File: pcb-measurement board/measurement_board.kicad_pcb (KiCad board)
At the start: 4 copper layers, 60 x 45 mm, 78 parts, among them P1 CONN_02X15, P2 CONN_02X13, P3 HDR DUAL ROW, P4 CONN_02X05, P5 CONN_02X05, Q2 Si1101X, U1 TPS73125, U10 AD8603, U11 TLV1G125, U12 MCP4921, U13 TPS73133, U14 MCP4921, U15 74CBTLV3253, U16 AD8293, U17 NX3L4051, U18 NX3L4051, U19 QS4A110, U2 NX3L4051, U20 QS4A110, U21 QS4A110, U3 NX3L4051, U4 NX3L4051, U5 MSP430G2955, U6 TLV1G125, U7 NX3L4051, U8 AD8603, U9 TLV1G125

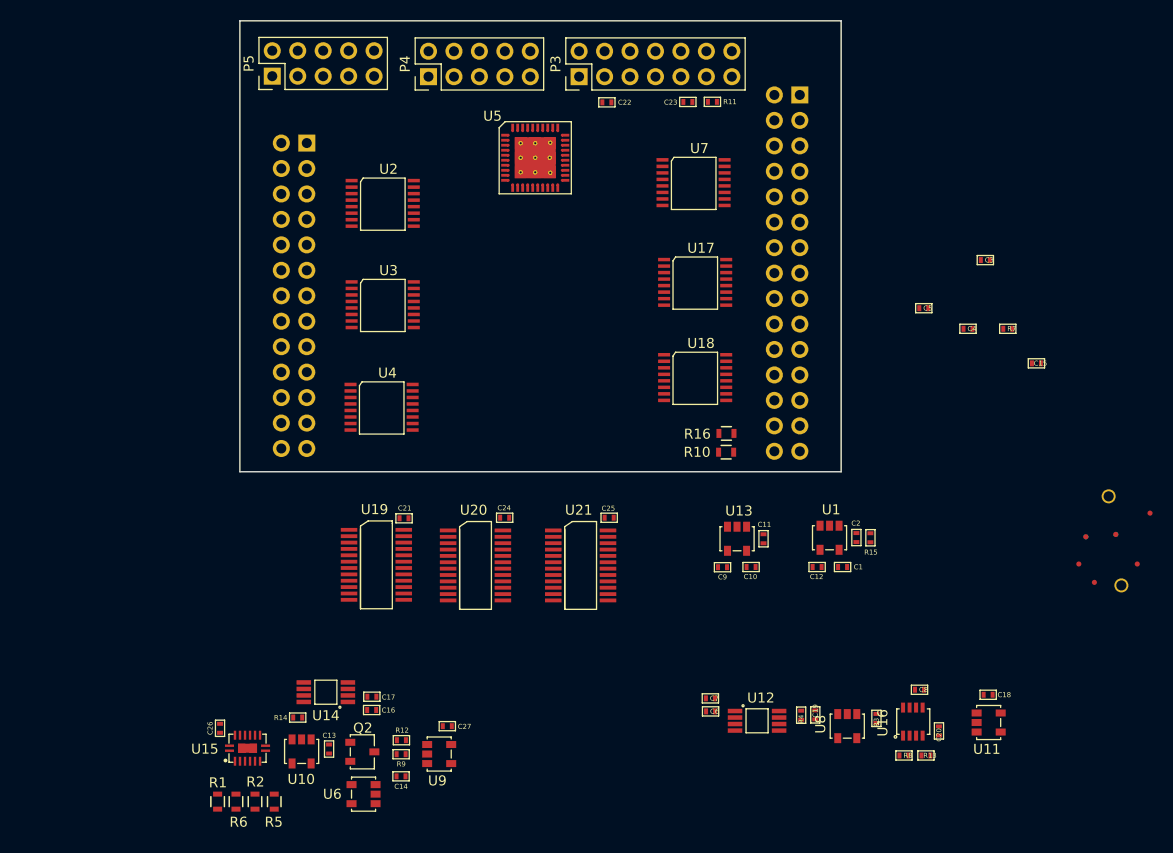
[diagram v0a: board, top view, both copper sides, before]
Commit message: -component placement completed -routing just started
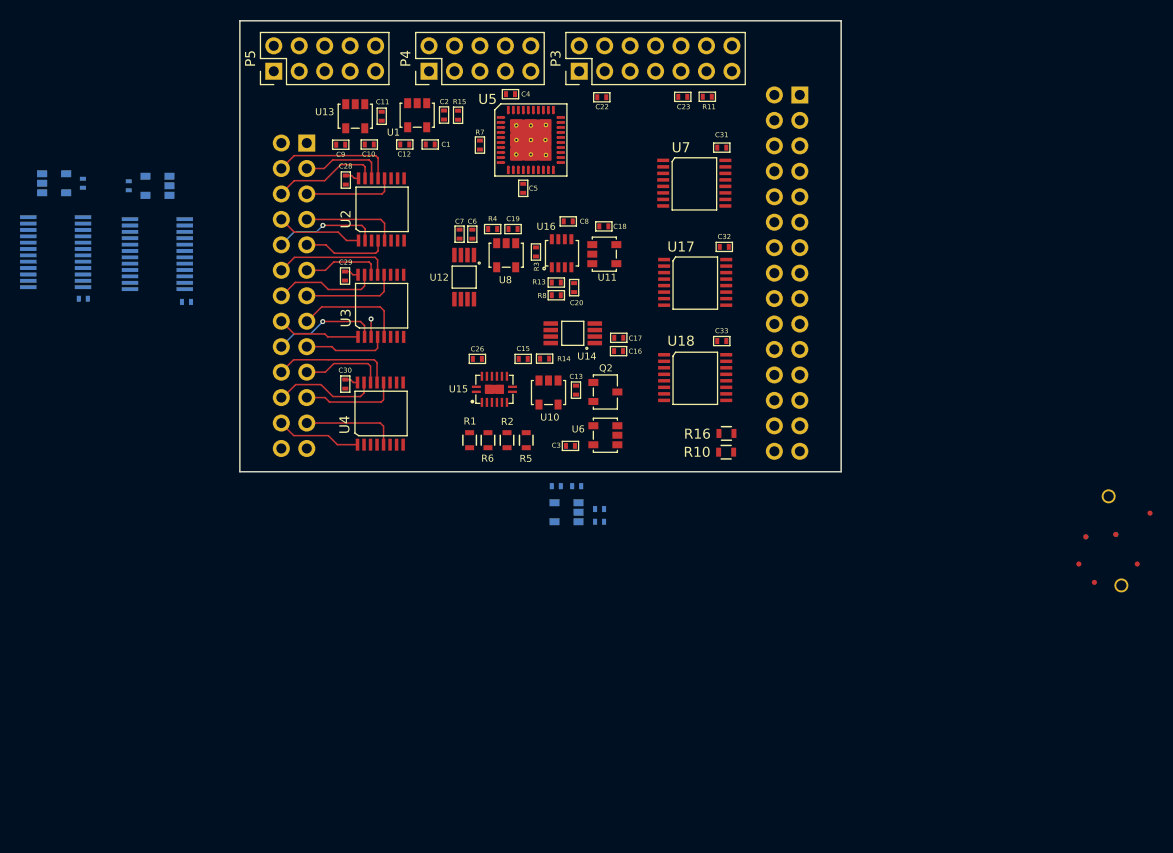
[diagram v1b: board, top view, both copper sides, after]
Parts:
- added C28: 0.1uF, footprints_on_Cdrive:0402, F.Cu at (-19.4, -9.11)
- added C29: 0.1uF, footprints_on_Cdrive:0402, F.Cu at (-19.5, 0.47)
- added C30: 0.1uF, footprints_on_Cdrive:0402, F.Cu at (-19.5, 11.3)
- added C31: 0.1uF, footprints_on_Cdrive:0402, F.Cu at (18.1, -12.3)
- added C32: 0.1uF, footprints_on_Cdrive:0402, F.Cu at (18.3, -2.44)
- added C33: 0.1uF, footprints_on_Cdrive:0402, F.Cu at (18.1, 6.96)
- added C34: 0.1uF, footprints_on_Cdrive:0402, B.Cu at (-41.1, -8.53)
- added U22: TLV1G125, footprints_on_Cdrive:SOT23-5, B.Cu at (-37.0, -8.53)
- C14, C21, C24, C25, C27, R12, R9, U19, U20, U9: moved to B.Cu
- U21: value QS4A110 -> TLV1G125; footprint footprints_on_Cdrive:QSOP-24 -> footprints_on_Cdrive:SOT23-5; moved to B.Cu
- moved C25 62.2 mm to (-45.7, -8.79), turned to 270 degrees
- moved U21 61.7 mm to (-49.7, -8.79)
- moved C18 60.5 mm to (6.31, -4.48)
- moved U11 60.5 mm to (5.16, -1.71)
- moved R13 59.9 mm to (1.57, 1.12), turned to 180 degrees
- moved C2 58.9 mm to (-9.63, -15.6)
- moved U1 58.9 mm to (-12.3, -16.8)
- moved C1 58.9 mm to (-11.0, -12.7)
- moved C12 58.9 mm to (-13.5, -12.7)
- moved R15 58.9 mm to (-8.23, -15.6)
- moved C8 58.4 mm to (2.77, -4.98)
- moved U16 58.4 mm to (1.13, -1.80)
- moved U8 58.0 mm to (-3.43, -2.81)
- moved R3 57.6 mm to (-0.46, -1.93)
- moved R8 57.6 mm to (1.57, 2.39)
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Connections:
- net Net-(U11-Pad4) renamed /Vmeas
- C25 pad 1: /5V -> /3V3
- U20 pad 11: /O2 -> /P2
- U20 pad 14: /P2 -> /Q2
- U20 pad 17: /Q2 -> /R2
- U20 pad 18: /R2 -> /S2
- U20 pad 21: /S2 -> /T2
- U20 pad 22: /T2 -> /U2
- U20 pad 3: /K2 -> /L2
- U20 pad 4: /L2 -> /M2
- U20 pad 7: /M2 -> /N2
- U20 pad 8: /N2 -> /O2
- U21 pad 2: GND -> /K2
- U21 pad 3: /U2 -> GND
- U21 pad 4: /V2 -> GND
- U21 pad 5: GND -> /3V3
- U5 pad 12: /MUX2 -> Net-(U5-Pad12)
- U5 pad 16: /~CC_EN -> /~MUX_EN1
- U5 pad 17: Net-(U5-Pad17) -> /~CC_EN
- U5 pad 2: /~MUX_EN5 -> /~MUX_EN2
- U5 pad 22: Net-(U5-Pad22) -> /DAC1_CS
- U5 pad 25: /~MUX_EN3 -> /Imeas
- U5 pad 26: /~MUX_EN2 -> /ADC_IN
- U5 pad 27: /~MUX_EN1 -> /~MUX_EN3
- U5 pad 40: /DAC1_CS -> /~MUX_EN5
- U5 pad 6: /Imeas -> /MUX0
- U5 pad 7: /MUX0 -> /MUX1
- U5 pad 8: /MUX1 -> /MUX2
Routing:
- net /A1: track 0.00 -> 12.3 mm
- net /I1: track 0.00 -> 12.2 mm
- net /E1: track 0.00 -> 11.7 mm
- net /G2: track 0.00 -> 11.1 mm
- net /B1: track 0.00 -> 10.8 mm
- net /H1: track 0.00 -> 10.6 mm, vias 0 -> 1
- net /D1: track 0.00 -> 10.5 mm, vias 0 -> 1
- net /J1: track 0.00 -> 10.5 mm
- net /F1: track 0.00 -> 10.4 mm
- net /J2: track 0.00 -> 9.66 mm
- net /C2: track 0.00 -> 9.64 mm
- net /K2: track 0.00 -> 9.63 mm
- net /F2: track 0.00 -> 9.57 mm
- net /B2: track 0.00 -> 9.17 mm
- net /D2: track 0.00 -> 8.59 mm
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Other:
- net class Default: via_dia 0.6858 -> 0.508; via_drill 0.3302 -> 0.254
- rule via_min_drill: 0.3302 -> 0.254
- rule via_min_size: 0.6858 -> 0.508

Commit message: -replaced all measurement board 0402 components with 0603 -adjusted placement and started routing on the layout
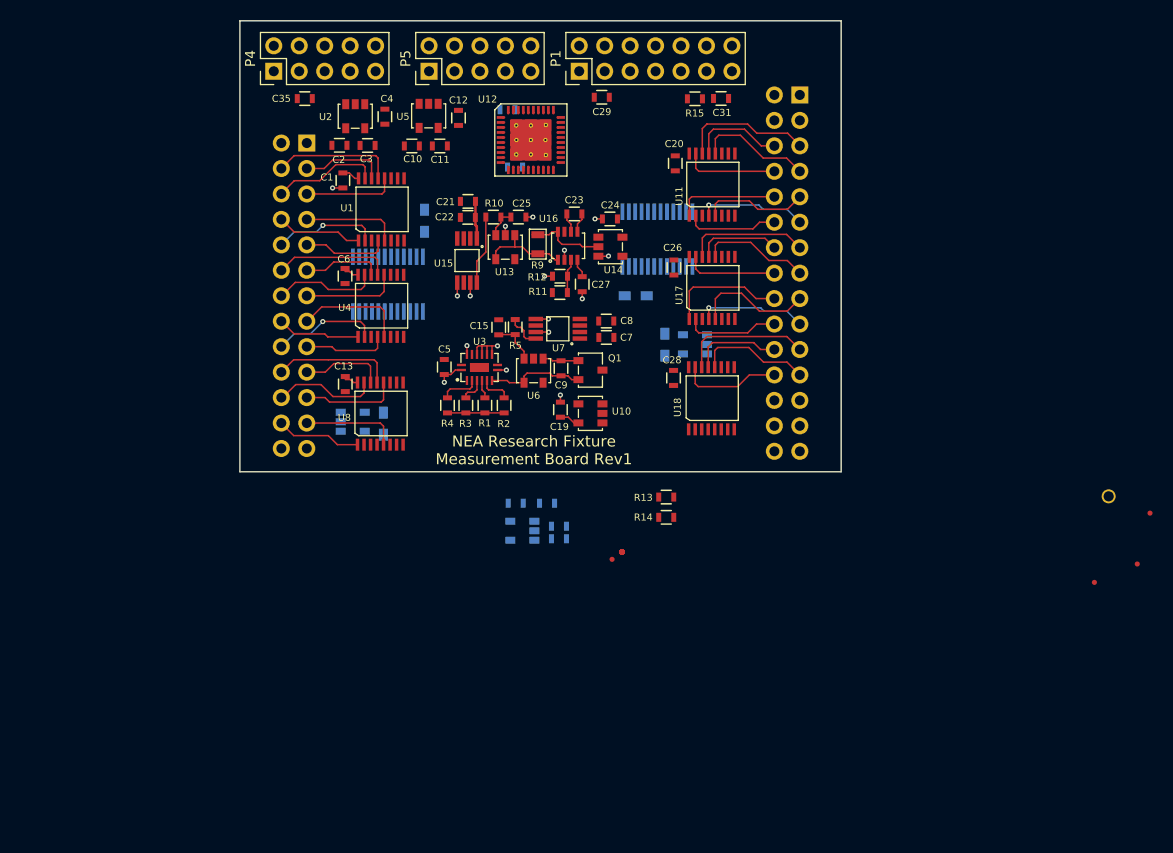
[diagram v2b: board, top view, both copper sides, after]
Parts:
- removed the R13 at (1.57, 1.12)
- removed the R14 at (0.41, 8.72)
- removed the R3 at (-0.46, -1.93)
- removed the R4 at (-4.78, -4.22)
- removed R8: 100k, footprints_on_Cdrive:0402
- removed the TP2 at (54.4, 26.5)
- removed the TP3 at (57.4, 26.3)
- removed the TP6 at (58.0, 31.3)
- added C35: 10uF, footprints_on_Cdrive:0603, F.Cu at (-23.5, -17.2)
- added R10: 1K, footprints_on_Cdrive:0603, F.Cu at (-4.71, -5.41)
- added R5: 1K, footprints_on_Cdrive:0603, F.Cu at (-2.52, 5.56)
- added R6: 1K, footprints_on_Cdrive:0603, B.Cu at (1.84, 25.4)
- added TP10, TP11, TP12, TP13, TP14, TP15, TP4, TP7, TP8, TP9: TP_SMT, footprints_on_Cdrive:TP_SMT.02, F.Cu at (8.13, 28.0)
- C1: value 0.47uF -> 0.1uF; footprint footprints_on_Cdrive:0402 -> footprints_on_Cdrive:0603
- C10, C2: value 0.47uF -> DNI; footprint footprints_on_Cdrive:0402 -> footprints_on_Cdrive:0603
- C11, C15, C19, C26, C28, C5, C8: footprint footprints_on_Cdrive:0402 -> footprints_on_Cdrive:0603
- C12: value DNI -> 0.47uF; footprint footprints_on_Cdrive:0402 -> footprints_on_Cdrive:0603
- C13: value 51pF -> 0.1uF; footprint footprints_on_Cdrive:0402 -> footprints_on_Cdrive:0603
- C14: value 1nF -> 1.1nF; footprint footprints_on_Cdrive:0402 -> footprints_on_Cdrive:0603
- C16: value 10uF -> 0.1uF; footprint footprints_on_Cdrive:0402 -> footprints_on_Cdrive:0603; moved to B.Cu
- C17, C18: footprint footprints_on_Cdrive:0402 -> footprints_on_Cdrive:0603; moved to B.Cu
- C20: value 39nF -> 0.1uF; footprint footprints_on_Cdrive:0402 -> footprints_on_Cdrive:0603
- C21: value 0.1uF -> 10uF; footprint footprints_on_Cdrive:0402 -> footprints_on_Cdrive:0603; moved to F.Cu
- C22, C6: value 10uF -> 0.1uF; footprint footprints_on_Cdrive:0402 -> footprints_on_Cdrive:0603
- C23: value 1.1nF -> 0.1uF; footprint footprints_on_Cdrive:0402 -> footprints_on_Cdrive:0603
- C24, C25: footprint footprints_on_Cdrive:0402 -> footprints_on_Cdrive:0603; moved to F.Cu
- C27: value 0.1uF -> 39nF; footprint footprints_on_Cdrive:0402 -> footprints_on_Cdrive:0603; moved to F.Cu
- C29, C7: value 0.1uF -> 10uF; footprint footprints_on_Cdrive:0402 -> footprints_on_Cdrive:0603
- C3, C4: value 0.1uF -> 0.47uF; footprint footprints_on_Cdrive:0402 -> footprints_on_Cdrive:0603
- C30, C32, C33: footprint footprints_on_Cdrive:0402 -> Resistors_SMD:R_0603_HandSoldering; moved to B.Cu
- C31: value 0.1uF -> 1.1nF; footprint footprints_on_Cdrive:0402 -> footprints_on_Cdrive:0603
- C34: footprint footprints_on_Cdrive:0402 -> Resistors_SMD:R_0603_HandSoldering
- C9: value DNI -> 51pF; footprint footprints_on_Cdrive:0402 -> footprints_on_Cdrive:0603
- R11: value 47K -> 100k; footprint footprints_on_Cdrive:0402 -> footprints_on_Cdrive:0603
- R12: value 100K -> 18k; footprint footprints_on_Cdrive:0402 -> footprints_on_Cdrive:0603; moved to F.Cu
- R15: value 1K -> 47K; footprint footprints_on_Cdrive:0402 -> footprints_on_Cdrive:0603
- R7: value 47K -> 100k; footprint footprints_on_Cdrive:0402 -> footprints_on_Cdrive:0603; moved to B.Cu
- R9: value 1K -> 10ohm 0.1%; footprint footprints_on_Cdrive:0402 -> footprints_on_Cdrive:0805; moved to F.Cu
- moved U22 55.9 mm to (16.6, 7.29)
- moved C34 55.8 mm to (12.4, 7.33), turned to 270 degrees
- moved U20 49.7 mm to (8.17, -5.95), turned to 0 degrees
- moved TP1 46.6 mm to (7.14, 28.7)
- moved C25 43.6 mm to (-2.21, -5.41), turned to 0 degrees
- moved C24 43.1 mm to (6.92, -5.23)
- moved C21 39.6 mm to (-7.24, -6.98)
- moved U19 39.4 mm to (-11.7, 4.01), turned to 180 degrees
- moved C28 38.2 mm to (13.3, 10.6), turned to 270 degrees
- moved U21 38.1 mm to (-19.9, 15.0)
- moved R7 36.4 mm to (0.65, 23.1), turned to 180 degrees
- moved C3 36.2 mm to (-17.3, -12.6), turned to 180 degrees
- moved C33 34.8 mm to (-15.7, 15.2), turned to 90 degrees
- moved C9 31.3 mm to (2.05, 9.68), turned to 90 degrees
- moved C29 31.2 mm to (6.11, -17.4), turned to 180 degrees
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- renumbered P3 to P1, P1 to P2, P2 to P3, P5 to P4, P4 to P5, Q2 to Q1, R2 to R1, R16 to R13, R10 to R14, R5 to R2, R6 to R3, R1 to R4, TP19 to TP2, TP11 to TP3, TP4 to TP6, U2 to U1, U6 to U10, U7 to U11, U5 to U12, U8 to U13, U11 to U14, U12 to U15, U13 to U2, U15 to U3, U3 to U4, U1 to U5, U10 to U6, U14 to U7, U4 to U8
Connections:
- C1 pad 1: /V2P5 -> /3V3
- C10 pad 1: /3V3 -> Net-(C10-Pad1)
- C11 pad 1: /VIN -> /V2P5
- C12 pad 1: Net-(C12-Pad1) -> /3V3
- C13 pad 1: /BIAS_OUT -> /3V3
- C13 pad 2: Net-(C13-Pad2) -> GND
- C19 pad 1: Net-(C19-Pad1) -> /3V3
- C2 pad 1: /3V3 -> Net-(C2-Pad1)
- C20 pad 1: /Imeas -> /3V3
- C21 pad 1: /5V -> /3V3
- C23 pad 1: /~RST -> Net-(C23-Pad1)
- C23 pad 2: GND -> Net-(C23-Pad2)
- C24 pad 1: /5V -> /3V3
- C25 pad 1: /3V3 -> Net-(C25-Pad1)
- C27 pad 1: /3V3 -> /Imeas
- C30 pad 1: /3V3 -> /5V
- C31 pad 1: /3V3 -> /~RST
- C32 pad 1: /3V3 -> /5V
- C4 pad 1: /3V3 -> /5V
- C8 pad 1: Net-(C8-Pad1) -> /3V3
- C8 pad 2: Net-(C8-Pad2) -> GND
- C9 pad 1: Net-(C9-Pad1) -> /BIAS_OUT
- C9 pad 2: GND -> Net-(C9-Pad2)
- Q1 pad 1: Net-(C13-Pad2) -> Net-(C9-Pad2)
- R11 pad 1: /3V3 -> /0V5
- R11 pad 2: /~RST -> /3V3
- R12 pad 1: /~SELG -> GND
- R12 pad 2: GND -> /0V5
- R15 pad 1: /V2P5 -> /~RST
- R15 pad 2: /V2P5_R -> /3V3
- R7 pad 1: /~RST -> GND
- R7 pad 2: /3V3 -> /~SELG
- R9 pad 2: Net-(C14-Pad1) -> Net-(R9-Pad2)
- TP1 pad 1: Net-(TP1-Pad1) -> /3V3
- TP5 pad 1: /SIMO -> GND
- TP6 pad 1: Net-(C19-Pad1) -> Net-(C25-Pad1)
- U13 pad 1: Net-(R3-Pad2) -> Net-(R9-Pad2)
- U13 pad 3: Net-(C19-Pad1) -> Net-(C25-Pad1)
- U13 pad 4: Net-(R3-Pad2) -> Net-(R9-Pad2)
- U14 pad 2: Net-(R3-Pad1) (its old number) -> Net-(R9-Pad1)
- U16 pad 1: Net-(R3-Pad2) -> Net-(R9-Pad2)
- U16 pad 5: Net-(C8-Pad1) -> Net-(C23-Pad2)
- U16 pad 6: Net-(C8-Pad2) -> Net-(C23-Pad1)
- U16 pad 8: Net-(R3-Pad1) (its old number) -> Net-(R9-Pad1)
- U2 pad 1: /VIN -> /5V
- U2 pad 3: /VIN -> /5V
- U2 pad 4: Net-(C9-Pad1) -> Net-(C2-Pad1)
- U5 pad 4: Net-(C12-Pad1) -> Net-(C10-Pad1)
- U6 pad 1: Net-(C13-Pad2) -> Net-(C9-Pad2)
- U9 pad 2: Net-(R9-Pad1) -> Net-(R6-Pad2)
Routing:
- net GND: track 0.00 -> 22.7 mm, vias 0 -> 17
- net /M2: track 0.00 -> 13.3 mm
- net /U2: track 0.00 -> 13.1 mm
- net /Q2: track 0.00 -> 12.3 mm
- net /S2: track 0.00 -> 11.9 mm
- net /S1: track 0.00 -> 11.9 mm
- net /N2: track 0.00 -> 11.5 mm
- net /V2: track 0.00 -> 11.4 mm
- net /R2: track 0.00 -> 11.0 mm
- net /T2: track 0.00 -> 10.9 mm, vias 0 -> 1
- net /P2: track 0.00 -> 10.9 mm, vias 0 -> 1
- net /O2: track 0.00 -> 10.6 mm
- net /O1: track 0.00 -> 10.2 mm
- net /V1: track 0.00 -> 10.1 mm
- net /BIAS_OUT: track 0.00 -> 9.76 mm
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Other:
- board text added: "NEA Research Fixture Measurement Board Rev1"

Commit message: -more progress on the measurement board layout
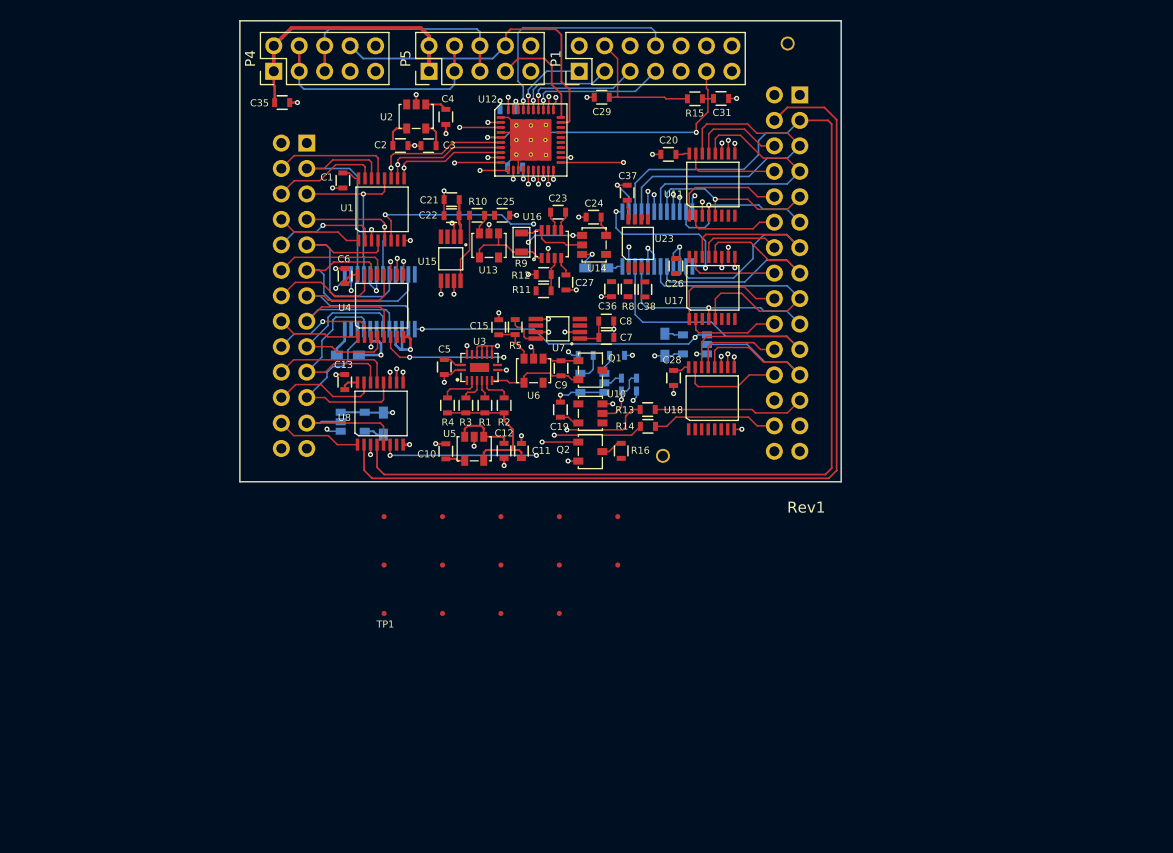
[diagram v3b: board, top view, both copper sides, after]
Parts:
- added C36: 0.1uF, footprints_on_Cdrive:0603, F.Cu at (7.09, 1.78)
- added C37: 0.1uF, footprints_on_Cdrive:0603, F.Cu at (8.65, -7.84)
- added C38: 1nF, footprints_on_Cdrive:0603, F.Cu at (10.4, 1.80)
- added Q2: 2N7002, footprints_on_Cdrive:SOT23, F.Cu at (6.17, 18.0)
- added R16: 47K, footprints_on_Cdrive:0603, F.Cu at (8.05, 17.9)
- added R8: 1K, footprints_on_Cdrive:0603, F.Cu at (8.74, 1.78)
- added TP16: header_pin, footprints_on_Cdrive:Header_Pin_Rnd, F.Cu at (24.7, -22.7)
- added U23: AD7683, footprints_on_Cdrive:RM-8, F.Cu at (8.76, -0.38)
- moved TP6 76.4 mm to (-15.6, 24.5)
- moved TP3 75.2 mm to (-15.6, 29.3)
- moved TP2 65.4 mm to (-9.78, 24.5)
- moved TP5 44.7 mm to (12.2, 18.4)
- moved U5 33.5 mm to (-6.62, 16.5)
- moved C12 33.5 mm to (-3.64, 17.9)
- moved C11 31.5 mm to (-1.91, 17.9), turned to 90 degrees
- moved C10 30.7 mm to (-9.45, 18.0), turned to 90 degrees
- moved TP1 23.4 mm to (-15.6, 34.1)
- moved TP8 18.9 mm to (-9.78, 34.1)
- moved TP4 18.0 mm to (-9.78, 29.3)
- moved C14 16.3 mm to (8.82, 11.9)
- moved C18 16.3 mm to (4.51, 8.38)
- moved R6 16.3 mm to (8.82, 10.7)
- moved R7 16.3 mm to (7.64, 8.39)
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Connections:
- net Net-(C14-Pad1) renamed /CC
- U12 pad 11: /SCL -> /SCK
- U12 pad 12: Net-(U12-Pad12) -> /~MUX_EN3
- U12 pad 17: /~CC_EN -> /SELR0
- U12 pad 18: Net-(U12-Pad18) -> /~ADC_CS
- U12 pad 25: /Imeas -> /SELR1
- U12 pad 26: /ADC_IN -> /Vmeas
- U12 pad 27: /~MUX_EN3 -> /0V5
- U12 pad 28: /V2P5_R -> /V2P5
- U12 pad 29: /GPIO_A -> /GPIO_B
- U12 pad 3: /~MUX_EN6 -> /DAC2_CS
- U12 pad 30: /GPIO_B -> /GPIO_A
- U12 pad 32: /DAC2_CS -> /~MUX_EN6
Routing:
- net /L2: track 0.00 -> 108.6 mm
- net GND: track 22.7 -> 116.6 mm, vias 17 -> 61
- net /L1: track 0.00 -> 92.6 mm
- net /GND_SENSORS: track 0.00 -> 82.4 mm, vias 0 -> 7
- net /MUX0: track 0.00 -> 61.0 mm, vias 0 -> 6
- net /MUX1: track 0.00 -> 61.0 mm, vias 0 -> 6
- net /MUX2: track 0.00 -> 58.8 mm, vias 0 -> 6
- net /3V3: track 10.4 -> 57.6 mm, vias 0 -> 2
- net /~MUX_EN3: track 0.00 -> 45.3 mm, vias 0 -> 3
- net /~MUX_EN2: track 0.00 -> 38.9 mm, vias 0 -> 3
- net /SDA: track 0.00 -> 37.4 mm, vias 0 -> 1
- net /~CV_EN: track 0.00 -> 36.9 mm, vias 0 -> 4
- net /SCK: track 0.00 -> 36.2 mm, vias 0 -> 1
- net /LED_1: track 0.00 -> 35.6 mm, vias 0 -> 2
- net /LED_2: track 0.00 -> 35.2 mm, vias 0 -> 2
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- added copper zone on In1.Cu, net GND
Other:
- board size 60 x 45 mm -> 60 x 46 mm
- board text added: "Rev1"

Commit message: progress on the measurement board layout
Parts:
- moved TP14 47.0 mm to (8.98, -12.4)
- moved TP1 7.27 mm to (-15.5, 26.9)
- moved TP11 7.27 mm to (-3.87, 26.9)
- moved TP8 7.27 mm to (-9.70, 26.9)
- moved TP12 4.38 mm to (1.88, 24.9)
- moved TP15 4.38 mm to (7.71, 24.9)
- moved TP3 4.38 mm to (-15.6, 24.9)
- moved TP4 4.38 mm to (-9.78, 24.9)
- moved TP9 4.38 mm to (-3.95, 24.9)
- moved TP10 1.64 mm to (1.88, 22.8)
- moved TP13 1.64 mm to (7.71, 22.8)
- moved TP2 1.64 mm to (-9.78, 22.8)
- moved TP6 1.64 mm to (-15.6, 22.8)
- moved TP7 1.64 mm to (-3.95, 22.8)
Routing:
- net /Vmeas: track 27.0 -> 123.9 mm, vias 4 -> 12
- net /CLK: track 1.25 -> 88.8 mm, vias 1 -> 7
- net /SOMI: track 0.00 -> 78.9 mm, vias 0 -> 2
- net /5V: track 32.5 -> 109.5 mm, vias 0 -> 6
- net /SIMO: track 0.00 -> 69.6 mm, vias 0 -> 5
- net /~MUX_EN5: track 1.23 -> 65.4 mm, vias 1 -> 2
- net /~MUX_EN6: track 1.31 -> 58.6 mm, vias 1 -> 3
- net /V2P5: track 15.1 -> 71.8 mm, vias 0 -> 5
- net /MUX2: track 58.8 -> 98.7 mm, vias 6 -> 7
- net /SELR1: track 0.00 -> 34.7 mm, vias 0 -> 3
- net /~MUX_EN4: track 1.30 -> 35.5 mm, vias 1 -> 3
- net /MUX1: track 61.0 -> 95.0 mm
- net /MUX0: track 61.0 -> 86.6 mm, vias 6 -> 7
- net /SELR0: track 1.36 -> 24.7 mm, vias 1 -> 3
- net /~ADC_CS: track 0.85 -> 21.2 mm, vias 1 -> 3
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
